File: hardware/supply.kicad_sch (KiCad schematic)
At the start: 35 parts, among them IC4 ACT4533AYH-T, U2 4011, U3 4081, U4 4071, U7 LM1117-3.3

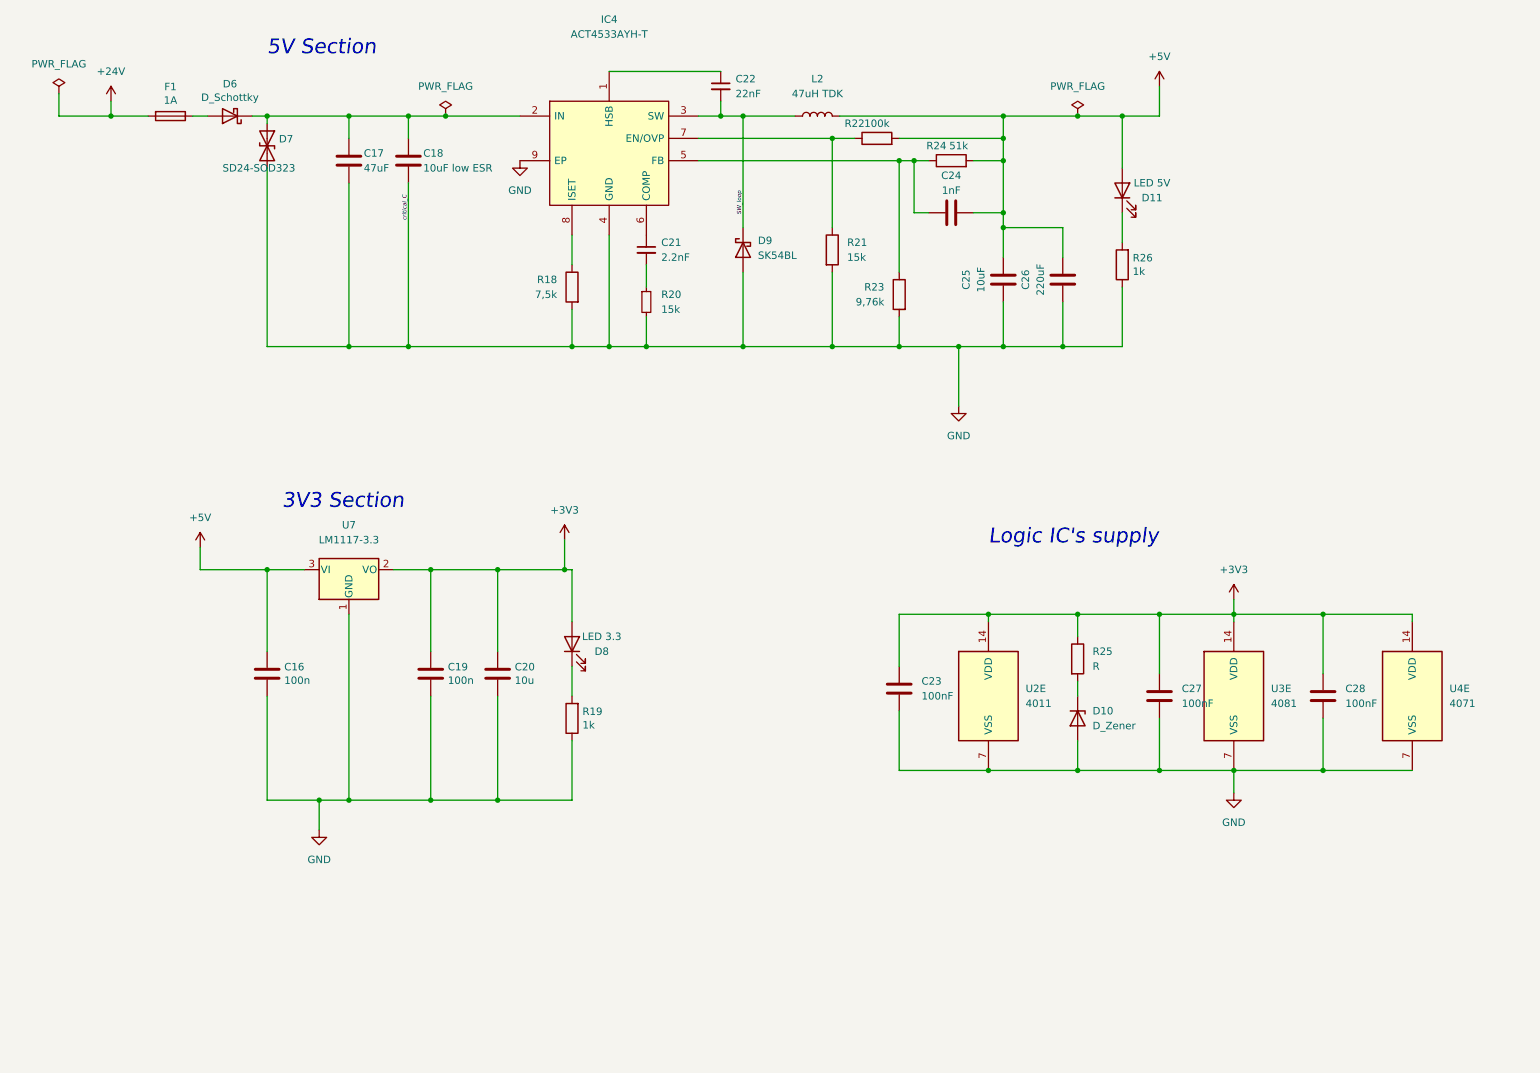
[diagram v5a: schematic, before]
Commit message: 0xERC State
Schematic needs only simulation and veryfying component choice for now
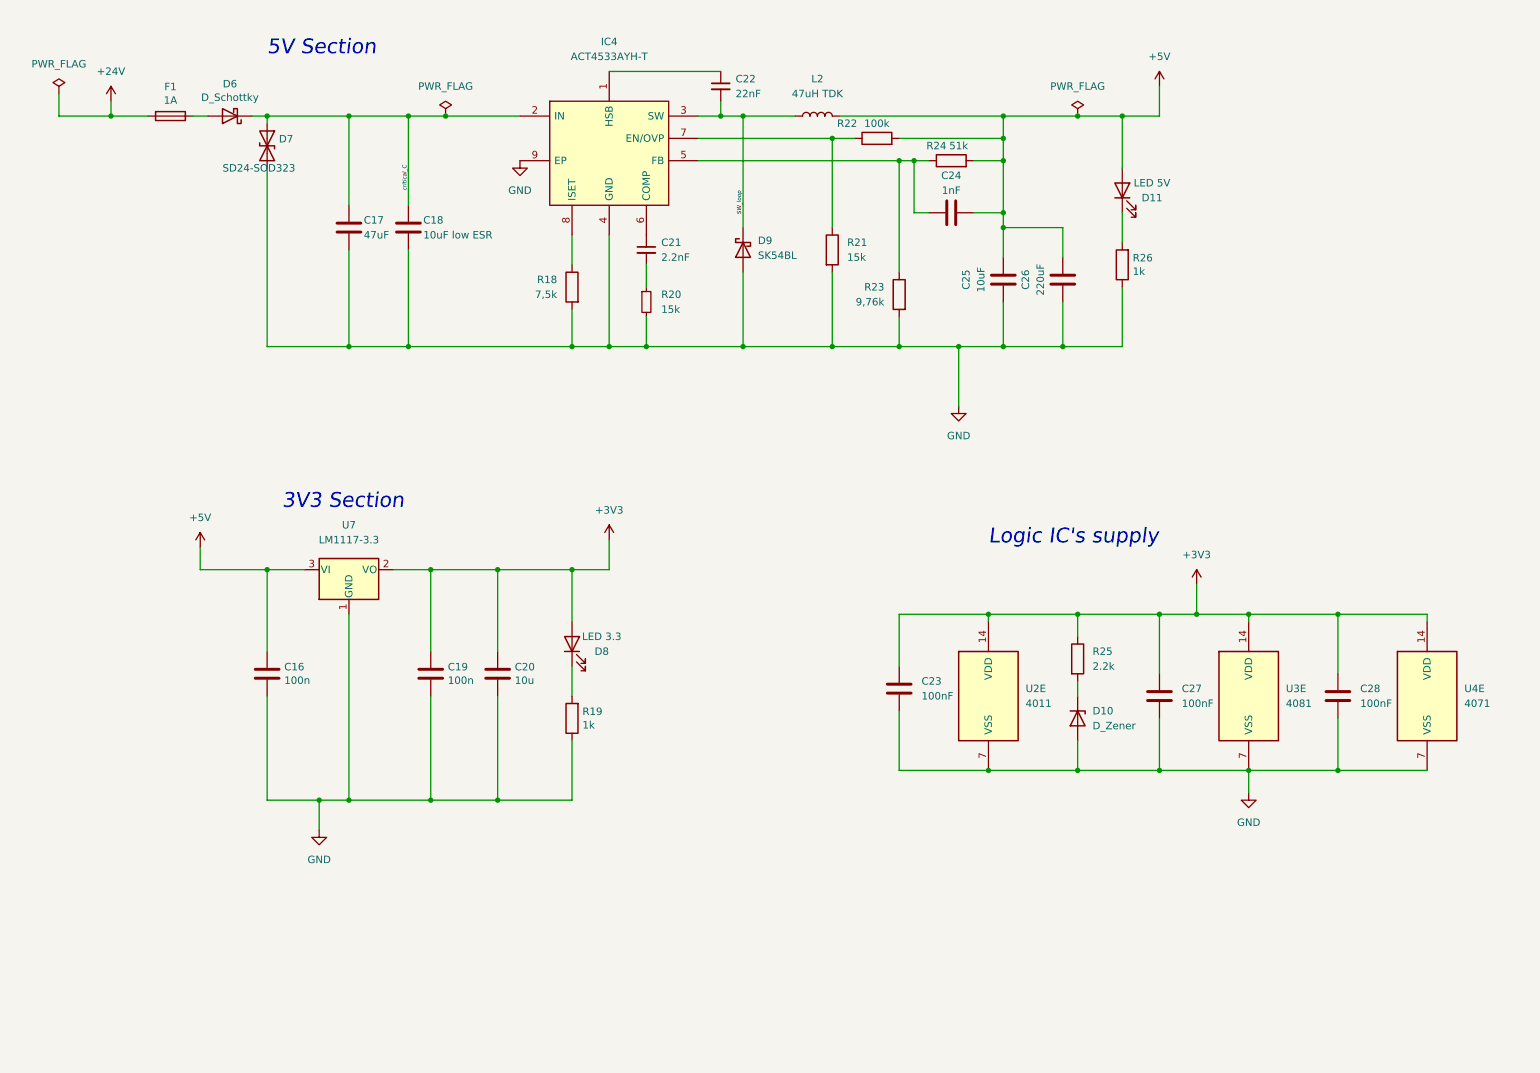
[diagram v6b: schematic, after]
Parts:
- R25: value R -> 2.2k
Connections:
- net critical_C: now reaches C17.1, C18.1, D6.1 (K), D7.1 (A1), IC4.2 (IN)
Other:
- moved on the sheet: C17, C18, C28, U3E, U4E

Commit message: working simulations, assigned footprints
"nightly" relase
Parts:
- U2, U3, U4: footprint (none) -> Package_SO:TSSOP-14_4.4x5mm_P0.65mm
- U7: footprint (none) -> Package_TO_SOT_SMD:TO-252-3_TabPin2
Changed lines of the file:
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@@
       (effects (font (size 1.27 1.27)) (justify left))
     )
-    (property "Footprint" "" (id 2) (at 259.08 130.81 0)
+    (property "Footprint" "Package_SO:TSSOP-14_4.4x5mm_P0.65mm" (id 2) (at 259.08 130.81 0)
       (effects (font (size 1.27 1.27)) hide)
     )
@@
       (effects (font (size 1.27 1.27)) (justify left))
     )
-    (property "Footprint" "" (id 2) (at 184.15 130.81 0)
+    (property "Footprint" "Package_SO:TSSOP-14_4.4x5mm_P0.65mm" (id 2) (at 184.15 130.81 0)
       (effects (font (size 1.27 1.27)) hide)
     )
@@
     (property "Reference" "U7" (id 0) (at 74.93 101.6 0))
     (property "Value" "LM1117-3.3" (id 1) (at 74.93 104.14 0))
-    (property "Footprint" "" (id 2) (at 74.93 109.22 0)
+    (property "Footprint" "Package_TO_SOT_SMD:TO-252-3_TabPin2" (id 2) (at 74.93 109.22 0)
       (effects (font (size 1.27 1.27)) hide)
     )
@@
       (effects (font (size 1.27 1.27)) (justify left))
     )
-    (property "Footprint" "" (id 2) (at 228.6 130.81 0)
-      (effects (font (size 1.27 1.27)) hide)
-    )
+    (property "Footprint" "Package_SO:TSSOP-14_4.4x5mm_P0.65mm" (id 2) (at 228.6 130.81 0)
+      (effects (font (size 1.27 1.27)) hide)
+    )

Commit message: kończymy balet na dziś
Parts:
- removed D6: D_Schottky, Diode_SMD:D_SMB, symbol Device:D_Schottky
- C16, C19, C20: footprint Capacitor_SMD:C_1206_3216Metric -> Capacitor_SMD:C_0603_1608Metric_Pad1.08x0.95mm_HandSolder
- C18: footprint Capacitor_SMD:C_1206_3216Metric -> Capacitor_SMD:C_0805_2012Metric_Pad1.18x1.45mm_HandSolder
- D10: value D_Zener -> BZX38450-C3V3-QX
- D11, D8: footprint LED_SMD:LED_PLCC-2 -> LED_SMD:LED_0603_1608Metric_Pad1.05x0.95mm_HandSolder
- L2: value 47uH TDK -> 47uH; footprint Inductor_SMD:L_1210_3225Metric -> PUTM_Kicad_FOOTPRINTS:L_Bourns_SRP1038WA
- R18, R20, R21, R22, R23, R24, R25: footprint Resistor_SMD:R_0603_1608Metric -> Resistor_SMD:R_0603_1608Metric_Pad0.98x0.95mm_HandSolder
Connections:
- net critical_C: now also F1.1
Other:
- note added: "SRP1038WA-470M"
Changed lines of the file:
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@@
-    (stroke (width 0) (type default) (color 0 0 0 0))
-  )
-  (wire (pts (xy 58.42 31.75) (xy 60.96 31.75))
     (stroke (width 0) (type default) (color 0 0 0 0))
   )
@@
     (stroke (width 0) (type default) (color 0 0 0 0))
   )
-  (wire (pts (xy 48.26 31.75) (xy 50.8 31.75))
+  (wire (pts (xy 48.26 31.75) (xy 60.96 31.75))
     (stroke (width 0) (type default) (color 0 0 0 0))
   )
@@
     (effects (font (size 2.54 2.54) italic) (justify left bottom))
   )
+  (text "SRP1038WA-470M" (at 148.59 24.13 0)
+    (effects (font (size 1.27 1.27) italic) (justify left bottom))
+  )
   (label "critical_C" (at 85.09 44.45 90)
     (effects (font (size 0.7 0.7) italic) (justify left bottom))
@@
       (effects (font (size 1.27 1.27)) (justify left))
     )
-    (property "Footprint" "Resistor_SMD:R_0603_1608Metric" (id 2) (at 155.702 54.61 90)
+    (property "Footprint" "Resistor_SMD:R_0603_1608Metric_Pad0.98x0.95mm_HandSolder" (id 2) (at 155.702 54.61 90)
       (effects (font (size 1.27 1.27)) hide)
     )
@@
       (effects (font (size 1.27 1.27)) (justify left))
     )
-    (property "Footprint" "Resistor_SMD:R_0603_1608Metric" (id 2) (at 125.73 63.5 0)
+    (property "Footprint" "Resistor_SMD:R_0603_1608Metric_Pad0.98x0.95mm_HandSolder" (id 2) (at 125.73 63.5 0)
       (effects (font (size 1.27 1.27)) hide)
     )
@@
     (property "Reference" "D11" (id 0) (at 212.09 45.72 90))
     (property "Value" "LED 5V" (id 1) (at 212.09 43.18 90))
-    (property "Footprint" "LED_SMD:LED_PLCC-2" (id 2) (at 207.01 44.45 0)
+    (property "Footprint" "LED_SMD:LED_0603_1608Metric_Pad1.05x0.95mm_HandSolder" (id 2) (at 207.01 44.45 0)
       (effects (font (size 1.27 1.27)) hide)
     )
@@
       (effects (font (size 1.27 1.27)) (justify left))
     )
-    (property "Footprint" "Capacitor_SMD:C_1206_3216Metric" (id 2) (at 86.0552 54.61 0)
+    (property "Footprint" "Capacitor_SMD:C_0805_2012Metric_Pad1.18x1.45mm_HandSolder" (id 2) (at 86.0552 54.61 0)
       (effects (font (size 1.27 1.27)) hide)
     )
@@
       (effects (font (size 1.27 1.27)) (justify left))
     )
-    (property "Value" "D_Zener" (id 1) (at 201.93 135.8899 90)
+    (property "Value" "BZX38450-C3V3-QX" (id 1) (at 201.93 135.8899 90)
       (effects (font (size 1.27 1.27)) (justify left))
     )
@@
       (effects (font (size 1.27 1.27)) (justify left))
     )
-    (property "Footprint" "Resistor_SMD:R_0603_1608Metric" (id 2) (at 114.808 60.96 90)
+    (property "Footprint" "Resistor_SMD:R_0603_1608Metric_Pad0.98x0.95mm_HandSolder" (id 2) (at 114.808 60.96 90)
       (effects (font (size 1.27 1.27)) hide)
     )
@@
       (effects (font (size 1.27 1.27)) (justify left))
     )
-    (property "Footprint" "Resistor_SMD:R_0603_1608Metric" (id 2) (at 170.688 62.23 90)
+    (property "Footprint" "Resistor_SMD:R_0603_1608Metric_Pad0.98x0.95mm_HandSolder" (id 2) (at 170.688 62.23 90)
       (effects (font (size 1.27 1.27)) hide)
     )
@@
     (property "Reference" "R24" (id 0) (at 175.26 36.83 90))
     (property "Value" "51k" (id 1) (at 179.07 36.83 90))
-    (property "Footprint" "Resistor_SMD:R_0603_1608Metric" (id 2) (at 177.8 41.148 90)
+    (property "Footprint" "Resistor_SMD:R_0603_1608Metric_Pad0.98x0.95mm_HandSolder" (id 2) (at 177.8 41.148 90)
       (effects (font (size 1.27 1.27)) hide)
     )
@@
       (effects (font (size 1.27 1.27)) (justify left))
     )
-    (property "Footprint" "Capacitor_SMD:C_1206_3216Metric" (id 2) (at 101.2952 130.81 0)
+    (property "Footprint" "Capacitor_SMD:C_0603_1608Metric_Pad1.08x0.95mm_HandSolder" (id 2) (at 101.2952 130.81 0)
       (effects (font (size 1.27 1.27)) hide)
     )
@@
       (effects (font (size 1.27 1.27)) (justify left))
     )
-    (property "Footprint" "Capacitor_SMD:C_1206_3216Metric" (id 2) (at 61.9252 130.81 0)
+    (property "Footprint" "Capacitor_SMD:C_0603_1608Metric_Pad1.08x0.95mm_HandSolder" (id 2) (at 61.9252 130.81 0)
       (effects (font (size 1.27 1.27)) hide)
     )
@@
     (pin "2")
   )
-  (symbol (lib_id "Device:D_Schottky") (at 54.61 31.75 180) (unit 1)
-    (in_bom yes) (on_board yes)
-    (property "Reference" "D6" (id 0) (at 54.61 26.2636 0))
-    (property "Value" "D_Schottky" (id 1) (at 54.61 28.575 0))
-    (property "Footprint" "Diode_SMD:D_SMB" (id 2) (at 54.61 31.75 0)
-      (effects (font (size 1.27 1.27)) hide)
-    )
-    (property "Datasheet" "~" (id 3) (at 54.61 31.75 0)
-      (effects (font (size 1.27 1.27)) hide)
-    )
-    (pin "1")
-    (pin "2")
-  )
   (symbol (lib_id "Device:R") (at 199.39 124.46 0) (unit 1)
     (in_bom yes) (on_board yes) (fields_autoplaced)
@@
       (effects (font (size 1.27 1.27)) (justify left))
     )
-    (property "Footprint" "Resistor_SMD:R_0603_1608Metric" (id 2) (at 197.612 124.46 90)
+    (property "Footprint" "Resistor_SMD:R_0603_1608Metric_Pad0.98x0.95mm_HandSolder" (id 2) (at 197.612 124.46 90)
       (effects (font (size 1.27 1.27)) hide)
     )
@@
     (property "Reference" "D8" (id 0) (at 118.11 123.19 90))
     (property "Value" "LED 3.3" (id 1) (at 118.11 120.65 90))
-    (property "Footprint" "LED_SMD:LED_PLCC-2" (id 2) (at 113.03 121.92 0)
+    (property "Footprint" "LED_SMD:LED_0603_1608Metric_Pad1.05x0.95mm_HandSolder" (id 2) (at 113.03 121.92 0)
       (effects (font (size 1.27 1.27)) hide)
     )
@@
       (effects (font (size 1.27 1.27)) (justify left))
     )
-    (property "Footprint" "Capacitor_SMD:C_1206_3216Metric" (id 2) (at 89.8652 130.81 0)
+    (property "Footprint" "Capacitor_SMD:C_0603_1608Metric_Pad1.08x0.95mm_HandSolder" (id 2) (at 89.8652 130.81 0)
       (effects (font (size 1.27 1.27)) hide)
     )
@@
     (property "Reference" "R22" (id 0) (at 160.02 33.02 90))
     (property "Value" "100k" (id 1) (at 165.1 33.02 90))
-    (property "Footprint" "Resistor_SMD:R_0603_1608Metric" (id 2) (at 165.1 37.338 90)
+    (property "Footprint" "Resistor_SMD:R_0603_1608Metric_Pad0.98x0.95mm_HandSolder" (id 2) (at 165.1 37.338 90)
       (effects (font (size 1.27 1.27)) hide)
     )
@@
     (in_bom yes) (on_board yes) (fields_autoplaced)
     (property "Reference" "L2" (id 0) (at 154.94 25.4 90))
-    (property "Value" "47uH TDK" (id 1) (at 154.94 27.94 90))
-    (property "Footprint" "Inductor_SMD:L_1210_3225Metric" (id 2) (at 154.94 31.75 0)
-      (effects (font (size 1.27 1.27)) hide)
-    )
+    (property "Value" "47uH " (id 1) (at 154.94 27.94 90))
+    (property "Footprint" "PUTM_Kicad_FOOTPRINTS:L_Bourns_SRP1038WA" (id 2) (at 154.94 31.75 0)
+      (effects (font (size 1.27 1.27)) hide)
+    )
